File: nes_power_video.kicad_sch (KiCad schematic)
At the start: 23 parts, among them J2 Audio, J3 Video, J4 Conn_01x05, J5 RGB conn feed, Q1 2SA1015, U1 TPS2553DBV

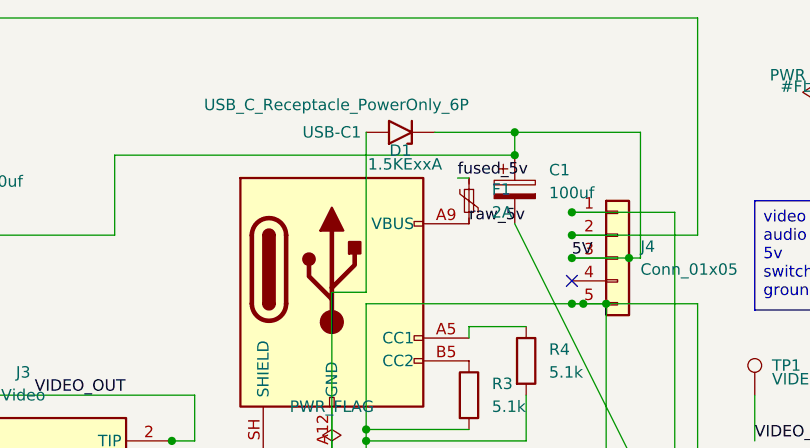
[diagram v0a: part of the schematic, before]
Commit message: Give every part a manufacturer, MPN, datasheet and supplier link
The TPS2553 verification from the last session only ever landed in a
gitignored datasheet PDF: the schematic still carried U1 as a bare
"TPS2553DBV" with an empty Datasheet field, and the exported fab BOM had
no manufacturer at all. That is the gap that let the EN-polarity question
stay open long enough to nearly buy the wrong part.

Every component instance now carries Manufacturer / MPN / LCSC /
Supplier Link / Datasheet fields, mirrored into BOM.csv as columns.
Jellybean passives get a Spec field (tolerance, rating, package) rather
than an invented part number - there is no MPN for a 220R axial resistor.

Specifics:
- U1: TPS2553DBVR, LCSC C55266, TI SLVS841F datasheet
- C3 / R6: pinned to JLCPCB basic parts C49678 and C17560; R6 keeps 1%
  because it sets the eFuse current limit
- Q1: datasheet was a dead datasheetcatalog.org link (404). Now onsemi
  KSA1015, which is what the BOM already told you to buy
- J2 / J3: datasheet moved off a Mouser link that no longer serves the
  PDF, onto Switchcraft's own drawing. Vendor field names normalised to
  Manufacturer / MPN
- USB-C1: datasheet was the generic USB-IF Type-C spec zip; now the GCT
  USB4970 drawing
- J2, J3 and J4 were missing from BOM.csv entirely
- D1's value read "1.5KExxA" - the KiCad symbol name, not a part you can
  order - in the schematic and on the silkscreen. Now 1.5KE6.8A, matching
  what the BOM has always said

Project-local symbol libraries carry the same fields so future
placements inherit them, and the cached lib_symbols were synced to match
(an unsynced cache raises lib_symbol_mismatch in ERC).

Verified: ERC 0 violations, check_nets.py all invariants pass, 14 nets
identical sch/pcb, DRC violation set unchanged from HEAD (7 pre-existing,
all J2/J3/TP1 silkscreen and courtyard from the jack rotation).

Co-Authored-By: Claude Opus 5 <noreply@anthropic.com>
Claude-Session: https://claude.ai/code/session_01SFPsiQ6ZtUgKSkh2NG4xCg
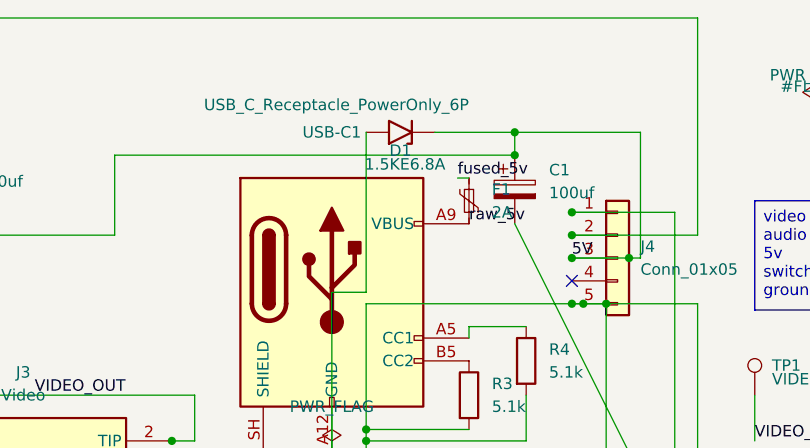
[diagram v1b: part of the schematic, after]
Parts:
- C1: Manufacturer (none) -> Generic; Spec (none) -> 100 uF, >=16 V, aluminium electrolytic, radial, <=10 mm dia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
- C2: Manufacturer (none) -> Generic; Spec (none) -> 470 uF, >=16 V, aluminium electrolytic, radial, <=10 mm dia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
- C3: LCSC (none) -> C49678; MPN (none) -> CC0805KRX7R9BB104; Manufacturer (none) -> YAGEO; Spec (none) -> 100 nF +/-10%, 50 V, X7R, 0805 (any equivalent >=16 V X7R); Supplier Link (none) -> https://www.lcsc.com/product-detail/C49678.html
- D1: value 1.5KExxA -> 1.5KE6.8A; MPN (none) -> 1.5KE6.8A; Manufacturer (none) -> Vishay; Supplier Link (none) -> https://www.digikey.com/en/products/result?keywords=1.5KE6.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
- F1: MPN (none) -> RHEF200; Manufacturer (none) -> Littelfuse; Spec (none) -> PPTC radial, IH 2.0 A / IT 3.8 A / 16 V max; Supplier Link (none) -> https://www.digikey.com/en/products/result?keywords=RHEF200
- J2, J3: MPN (none) -> PJRAN1X1U03X; Manufacturer (none) -> Switchcraft; Manufacturer_Name Switchcraft -> (none); Manufacturer_Part_Number PJRAN1X1U03X -> (none); Supplier Link (none) -> https://www.mouser.co.uk/ProductDetail/Switchcraft/PJRAN1X1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
- J4: Manufacturer (none) -> Generic; Spec (none) -> 1x05 pin header, 2.54 mm pitch, vertical THT (e.g. LCSC C49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
- J5: Manufacturer (none) -> Generic; Spec (none) -> 1x03 pin header, 2.54 mm pitch, vertical THT (e.g. LCSC C29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
- Q1: MPN (none) -> KSA1015; Manufacturer (none) -> onsemi; Spec (none) -> PNP TO-92, E-C-B pinout; any hFE grade. 2SA1015 is the obso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; Supplier Link (none) -> https://www.digikey.com/en/products/result?keywords=KSA1015
- R1: Manufacturer (none) -> Generic; Spec (none) -> 220 Ohm +/-5%, >=0.25 W, axial THT, 7.62 mm pitch
- R2: Manufacturer (none) -> Generic; Spec (none) -> 330 Ohm +/-5%, >=0.25 W, axial THT, 7.62 mm pitch
- R3, R4: Manufacturer (none) -> Generic; Spec (none) -> 5.1 kOhm +/-5%, >=0.1 W, axial THT, 7.62 mm pitch (USB-C CC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
- R5, R7: Manufacturer (none) -> Generic; Spec (none) -> 75 Ohm +/-1%, >=0.25 W, axial THT, 7.62 mm pitch
- R6: LCSC (none) -> C17560; MPN (none) -> 0805W8F2202T5E; Manufacturer (none) -> UNI-ROYAL; Spec (none) -> 22 kOhm +/-1%, 125 mW, 0805 - sets the eFuse current limit,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; Supplier Link (none) -> https://www.lcsc.com/product-detail/C17560.html
- TP1, TP2, TP3, TP4: Manufacturer (none) -> Not a purchased part; Spec (none) -> Bare plated through-hole pad, 2.0 mm pad / 1.0 mm drill
- U1: LCSC (none) -> C55266; MPN (none) -> TPS2553DBVR; Manufacturer (none) -> Texas Instruments; Supplier Link (none) -> https://www.lcsc.com/product-detail/C55266.html
- USB-C1: MPN (none) -> USB4970-00-A; Manufacturer (none) -> GCT; Spec (none) -> USB Type-C receptacle, 6P power-only (VBUS x2, GND x2, CC1,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; Supplier Link (none) -> https://www.digikey.com/en/products/result?keywords=USB4970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

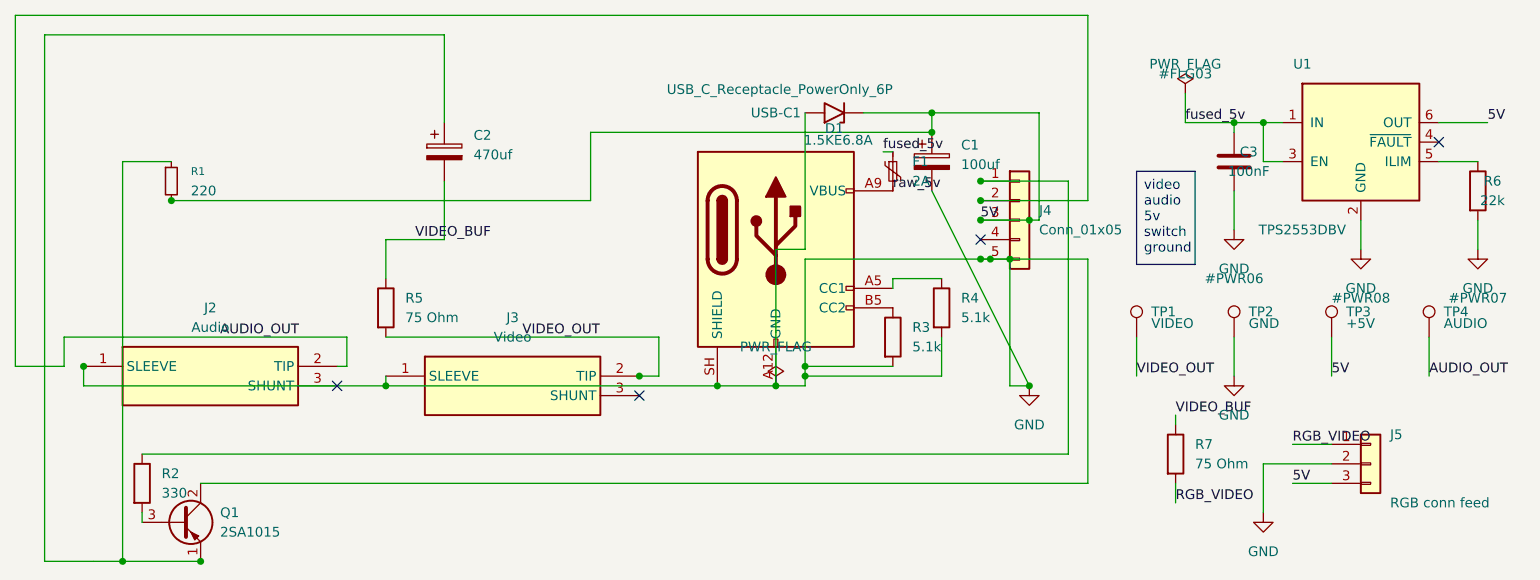
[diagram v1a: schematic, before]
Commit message: Fix Q1 silkscreen, USB-C footprint variant, and document F1's borrowed land pattern
Q1: the silkscreen printed 2SA1015, a discontinued part. It now prints
KSA1015, the onsemi part the BOM tells you to buy - same E-C-B pinout,
still in production. Schematic value and BOM value follow.

USB-C1: this was half a real bug. KiCad has no USB4970 footprint, but
GCT's USB4970 drawing specifies exactly the USB4125 land pattern - pad
centres 1.00/3.04/5.50 mm, widths 0.70/0.76/0.80 x 1.20 mm, shell holes
8.64 x 3.80 mm apart at 1.10 x 1.70 mm with 0.60 x 1.20 mm slots - which
is pad-for-pad what Connector_USB:USB_C_Receptacle_GCT_USB4125-xx-x
carries. So the copper was always right. What was wrong is the variant:
we had -0190, the 1.90 mm shell stake, while USB4970-00-A is the blank
suffix, 1.00 mm stake (GCT ordering grid). Switched to the plain
footprint, whose geometry is byte-identical apart from the name, descr
and 3D model, so not one pad moved. USB-C1's fab-layer value read
USB_C_Receptacle_PowerOnly_6P, a KiCad symbol name; now USB4970-00-A.

F1: no KiCad footprint exists for the Littelfuse RHEF series, so F1
borrows Fuse:Fuse_Bourns_MF-RG300 - pads at (0,0) and (5.1,1.2),
5.24 mm centre-to-centre, 1.01 mm drills. Per the RHEF datasheet the
RHEF200 has 0.51 mm (24 AWG) leads at 5.05 +/-0.75 mm spacing, so it
fits with room to spare. But the Bourns device is rated 3.0 A/5.1 A
against the RHEF200's 2.0 A/3.8 A, and the silkscreen outline is the
Bourns body - recorded as a Footprint Note field on F1, in BOM.csv and
in the README so nobody reads that outline as a clearance boundary.
Drawing a true RHEF200 footprint would move pad 2 by ~1.2 mm and force a
re-route, so it is a v3 change rather than a patch.

Verified: ERC 0 violations, check_nets.py all invariants pass, DRC
violation set identical to the previous commit, and the PCB diff is five
lines with no pad, track, via or zone touched.

Co-Authored-By: Claude Opus 5 <noreply@anthropic.com>
Claude-Session: https://claud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
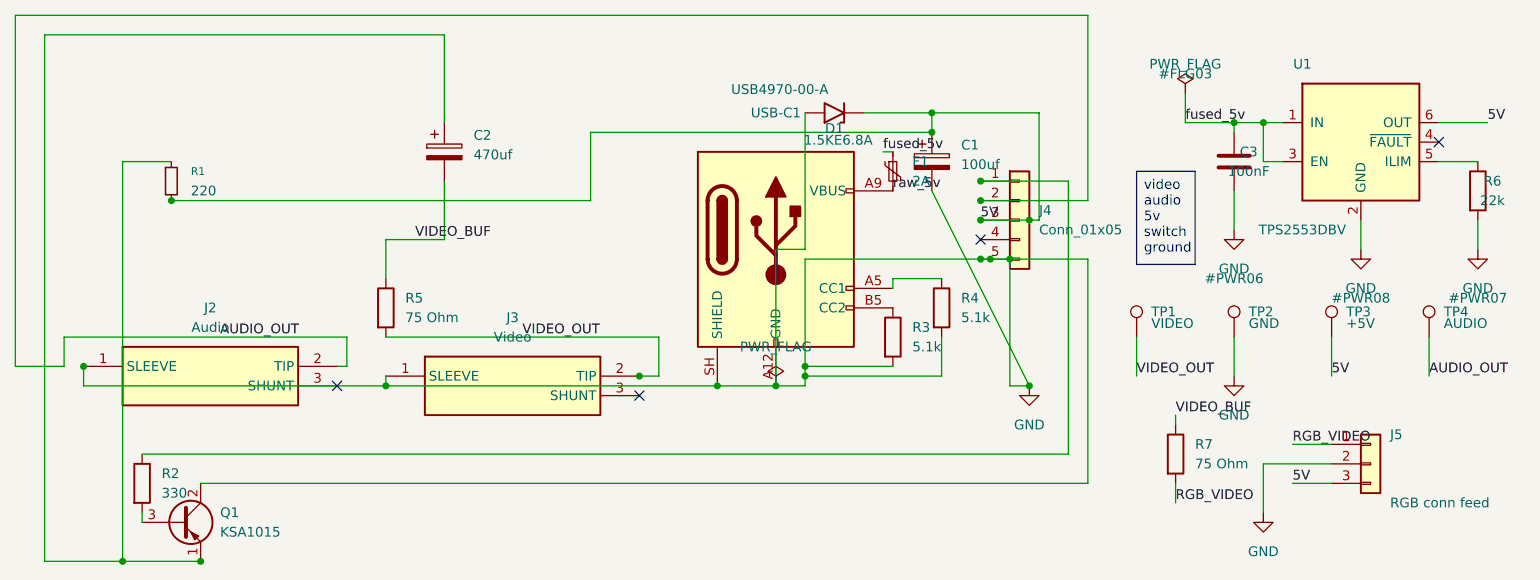
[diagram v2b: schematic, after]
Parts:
- F1: Footprint Note (none) -> No Littelfuse RHEF footprint exists in the KiCad libraries.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
- Q1: value 2SA1015 -> KSA1015
- USB-C1: value USB_C_Receptacle_PowerOnly_6P -> USB4970-00-A; footprint Connector_USB:USB_C_Receptacle_GCT_USB4125-xx-x-0190_6P_TopMnt_Horizontal -> Connector_USB:USB_C_Receptacle_GCT_USB4125-xx-x_6P_TopMnt_Horizontal; Footprint Note (none) -> KiCad has no USB4970 footprint. GCT's USB4970 drawing speci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
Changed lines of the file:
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@@
 			)
 		)
-		(property "Value" "2SA1015"
+		(property "Value" "KSA1015"
 			(at 40.64 190.4999 0)
 			(show_name no)
@@
 			)
 		)
+		(property "Footprint Note" "No Littelfuse RHEF footprint exists in the KiCad libraries. F1 uses the Bourns MF-RG300 land pattern: pads at (0,0) and (5.1,1.2), 5.24 mm centre-to-centre, 1.01 mm drills. RHEF200 leads are 0.51 mm dia at 5.05 +/-0.75 mm spacing, so they fit, but the Bourns part is a 3.0 A/5.1 A device and the drawn body outline is its, not the RHEF200's - do not trust the outline for clearance."
+			(at 128.27 143.51 0)
+			(hide yes)
+			(show_name no)
+			(do_not_autoplace no)
+			(effects
+				(font
+					(size 1.27 1.27)
+				)
+			)
+		)
 		(pin "1"
 		)
@@
 			)
 		)
-		(property "Value" "USB_C_Receptacle_PowerOnly_6P"
+		(property "Value" "USB4970-00-A"
 			(at 113.538 132.842 0)
 			(show_name no)
@@
 			)
 		)
-		(property "Footprint" "Connector_USB:USB_C_Receptacle_GCT_USB4125-xx-x-0190_6P_TopMnt_Horizontal"
+		(property "Footprint" "Connector_USB:USB_C_Receptacle_GCT_USB4125-xx-x_6P_TopMnt_Horizontal"
 			(at 116.84 151.13 0)
 			(hide yes)
@@
 			(at 113.03 153.67 0)
 			(hide yes)
+			(show_name no)
+			(do_not_autoplace no)
+			(effects
+				(font
+					(size 1.27 1.27)
+				)
+			)
+		)
+		(property "Footprint Note" "KiCad has no USB4970 footprint. GCT's USB4970 drawing specifies the same recommended layout as the USB4125: pad centres 1.00/3.04/5.50 mm, widths 0.70/0.76/0.80 mm x 1.20 mm, shell holes 8.64 x 3.80 mm apart, 1.10 x 1.70 mm with 0.60 x 1.20 mm slots. Verified against the drawing 2026-08-28. USB4970-00-A takes the 1.00 mm shell stake, so the plain USB4125-xx-x footprint is the match; -0190 is the 1.90 mm stake variant."
+			(at 113.03 153.67 0)
+			(hide yes)

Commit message: Replace search links with verified product pages; correct D1 and Q1 sourcing
With DigiKey and Mouser API access working, every supplier link is now a
real product page checked against live stock, and two of the parts turned
out to be specified wrong.

D1 was listed as Vishay 1.5KE6.8A. That is not an orderable MPN - Vishay
sells it as 1.5KE6.8A-E3/54, and the plain string belongs to Littelfuse,
which is the part actually being fitted. Switched to Littelfuse and
re-verified the numbers the README's "D1 does not protect U1" argument
rests on, since the cited datasheet changed: VWM 5.8 V, VBR 6.45 V min and
VC 10.5 V are identical, Ipp is 144.8 A rather than Vishay's 143 A. The
argument stands unchanged. Littelfuse packages it DO-201AA/DO-27 instead
of DO-201AE; the 15.24 mm footprint takes either.

Q1 is worse than the README claimed. It said the KSA1015 was "still in
production" - it is not. Every onsemi/Fairchild KSA1015 variant reads
Obsolete on DigiKey, stocked only as KSA1015GRTA-ON through Rochester
Electronics (11,217), the licensed last-time-buy channel. MCC's
2SA1015-GR-AP is genuine and in stock at Mouser (14,738) but flagged End
of Life. Both build the board today with deep stock; neither is in
production. Recorded in the schematic, BOM and README as a v3 item.

Also: F1 and USB-C1 keyword-search URLs replaced with product pages
(RHEF200HF-ND, 2073-USB4970-00-ATR-ND, both Active), and the Switchcraft
jacks moved from mouser.co.uk to mouser.com so every link points at one
storefront. DigiKey's datasheet URL for the RHEF200 came back identical
to the one committed earlier, which independently confirms that link.

Verified: ERC 0 violations, check_nets.py all invariants pass, PCB
untouched - this commit changes metadata only.

Co-Authored-By: Claude Opus 5 <noreply@anthropic.com>
Claude-Session: https://claude.ai/code/session_01SFPsiQ6ZtUgKSkh2NG4xCg
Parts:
- D1: Manufacturer Vishay -> Littelfuse; Spec (none) -> 1500 W unidirectional TVS: VWM 5.8 V, VBR 6.45 V min, VC 10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; Supplier Link https://www.digikey.com/en/products/result?keywords=1.5KE6.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 -> https://www.digikey.com/en/products/detail/littelfuse-inc/1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
- F1: Supplier Link https://www.digikey.com/en/products/result?keywords=RHEF200 -> https://www.digikey.com/en/products/detail/littelfuse-inc/R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
- J2, J3: Mouser Price/Stock https://www.mouser.co.uk/ProductDetail/Switchcraft/PJRAN1X1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 -> https://www.mouser.com/en/ProductDetail/Switchcraft/PJRAN1X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; Supplier Link https://www.mouser.co.uk/ProductDetail/Switchcraft/PJRAN1X1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 -> https://www.mouser.com/en/ProductDetail/Switchcraft/PJRAN1X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
- Q1: MPN KSA1015 -> KSA1015GRTA; Spec PNP TO-92, E-C-B pinout; any hFE grade. 2SA1015 is the obso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 -> PNP TO-92, E-C-B pinout, any hFE grade. END OF LIFE both wa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; Supplier Link https://www.digikey.com/en/products/result?keywords=KSA1015 -> https://www.digikey.com/en/products/detail/rochester-electr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
- USB-C1: Supplier Link https://www.digikey.com/en/products/result?keywords=USB4970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 -> https://www.digikey.com/en/products/detail/gct/USB4970-00-A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
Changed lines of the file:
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@@
 			)
 		)
-		(property "MPN" "KSA1015"
+		(property "MPN" "KSA1015GRTA"
 			(at 35.56 189.23 0)
 			(hide yes)
@@
 			)
 		)
-		(property "Spec" "PNP TO-92, E-C-B pinout; any hFE grade. 2SA1015 is the obsolete original"
+		(property "Spec" "PNP TO-92, E-C-B pinout, any hFE grade. END OF LIFE both ways: onsemi KSA1015 is obsolete, stocked only as KSA1015GRTA-ON through Rochester; MCC 2SA1015-GR-AP is on Mouser but flagged End of Life. Needs a live replacement for v3."
 			(at 35.56 189.23 0)
 			(hide yes)
@@
 			)
 		)
-		(property "Supplier Link" "https://www.digikey.com/en/products/result?keywords=KSA1015"
+		(property "Supplier Link" "https://www.digikey.com/en/products/detail/rochester-electronics-llc/KSA1015GRTA-ON/12643065"
 			(at 35.56 189.23 0)
 			(hide yes)
@@
 			)
 		)
-		(property "Supplier Link" "https://www.digikey.com/en/products/result?keywords=RHEF200"
+		(property "Supplier Link" "https://www.digikey.com/en/products/detail/littelfuse-inc/RHEF200/5130265"
 			(at 128.27 143.51 0)
 			(hide yes)
@@
 			)
 		)
-		(property "Datasheet" "https://www.vishay.com/docs/88301/15ke.pdf"
+		(property "Datasheet" "https://www.littelfuse.com/assetdocs/littelfuse_tvs_diode_1_5ke_datasheet.pdf?assetguid=9d02c7d2-86a5-4bff-9251-966d6af02bf7"
 			(at 121.92 135.89 0)
 			(hide yes)
@@
 			)
 		)
-		(property "Manufacturer" "Vishay"
+		(property "Manufacturer" "Littelfuse"
 			(at 121.92 135.89 0)
 			(hide yes)
@@
 			)
 		)
-		(property "Supplier Link" "https://www.digikey.com/en/products/result?keywords=1.5KE6.8A"
+		(property "Supplier Link" "https://www.digikey.com/en/products/detail/littelfuse-inc/1-5KE6-8A/285842"
+			(at 121.92 135.89 0)
+			(hide yes)
+			(show_name no)
+			(do_not_autoplace no)
+			(effects
+				(font
+					(size 1.27 1.27)
+				)
+			)
+		)
+		(property "Spec" "1500 W unidirectional TVS: VWM 5.8 V, VBR 6.45 V min, VC 10.5 V @ 144.8 A. Littelfuse packages it as DO-201AA/DO-27; the DO-201AE footprint takes it (15.24 mm pitch, 1.3 mm drills)."
 			(at 121.92 135.89 0)
 			(hide yes)
@@
 			)
 		)
-		(property "Mouser Price/Stock" "https://www.mouser.co.uk/ProductDetail/Switchcraft/PJRAN1X1U03X?qs=mcPJWgAPNrc45bmxqO8nXw%3D%3D"
+		(property "Mouser Price/Stock" "https://www.mouser.com/en/ProductDetail/Switchcraft/PJRAN1X1U03X?qs=mcPJWgAPNrc45bmxqO8nXw%3D%3D"
 			(at 91.44 765.1 0)
 			(hide yes)
@@
 			)
 		)
-		(property "Supplier Link" "https://www.mouser.co.uk/ProductDetail/Switchcraft/PJRAN1X1U03X?qs=mcPJWgAPNrc45bmxqO8nXw%3D%3D"
+		(property "Supplier Link" "https://www.mouser.com/en/ProductDetail/Switchcraft/PJRAN1X1U03X?qs=mcPJWgAPNrc45bmxqO8nXw%3D%3D"
 			(at 91.44 365.1 0)
 			(hide yes)
@@
 			)
 		)
-		(property "Supplier Link" "https://www.digikey.com/en/products/result?keywords=USB4970-00-A"
+		(property "Supplier Link" "https://www.digikey.com/en/products/detail/gct/USB4970-00-A/28722813"
 			(at 113.03 153.67 0)
 			(hide yes)
@@
 			)
 		)
-		(property "Mouser Price/Stock" "https://www.mouser.co.uk/ProductDetail/Switchcraft/PJRAN1X1U03X?qs=mcPJWgAPNrc45bmxqO8nXw%3D%3D"
+		(property "Mouser Price/Stock" "https://www.mouser.com/en/ProductDetail/Switchcraft/PJRAN1X1U03X?qs=mcPJWgAPNrc45bmxqO8nXw%3D%3D"
 			(at 52.07 763.83 0)
 			(hide yes)
@@
 			)
 		)
-		(property "Supplier Link" "https://www.mouser.co.uk/ProductDetail/Switchcraft/PJRAN1X1U03X?qs=mcPJWgAPNrc45bmxqO8nXw%3D%3D"
+		(property "Supplier Link" "https://www.mouser.com/en/ProductDetail/Switchcraft/PJRAN1X1U03X?qs=mcPJWgAPNrc45bmxqO8nXw%3D%3D"
 			(at 52.07 363.83 0)
 			(hide yes)
